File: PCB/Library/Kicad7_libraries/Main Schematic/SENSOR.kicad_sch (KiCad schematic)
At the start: 15 parts, among them Q1 2SC1815, Q2 2SC1815, U2 TMP100, U3 EA_T123X-I2C

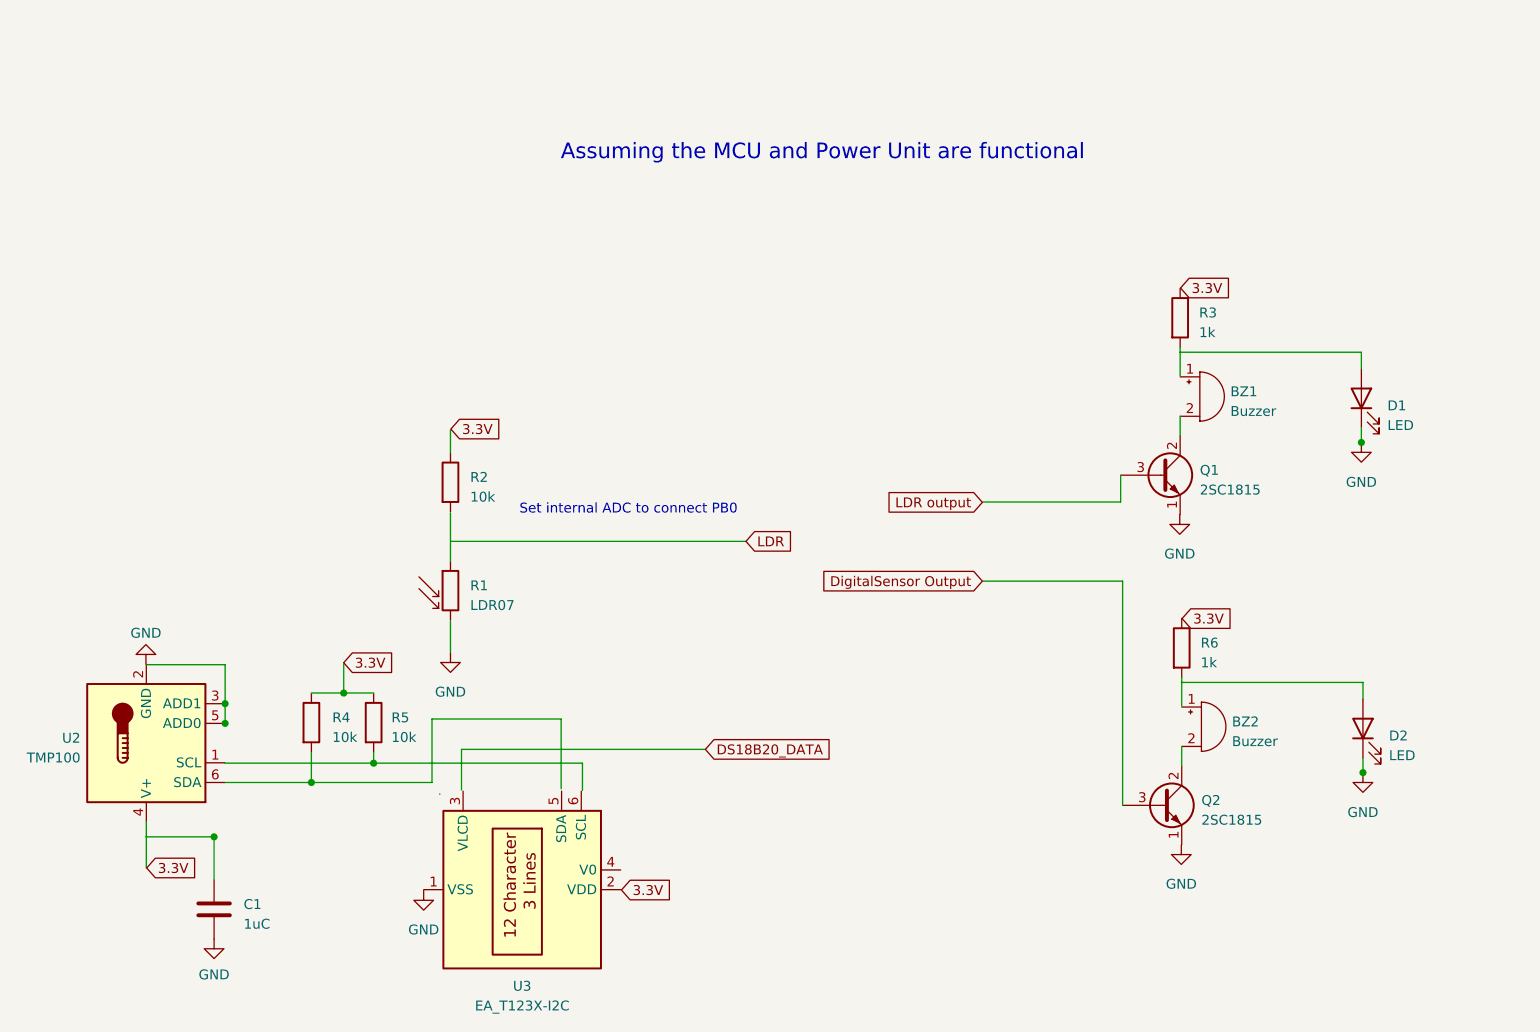
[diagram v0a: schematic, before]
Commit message: I recreated our schematics into hierachy sheets instead of individual sheets
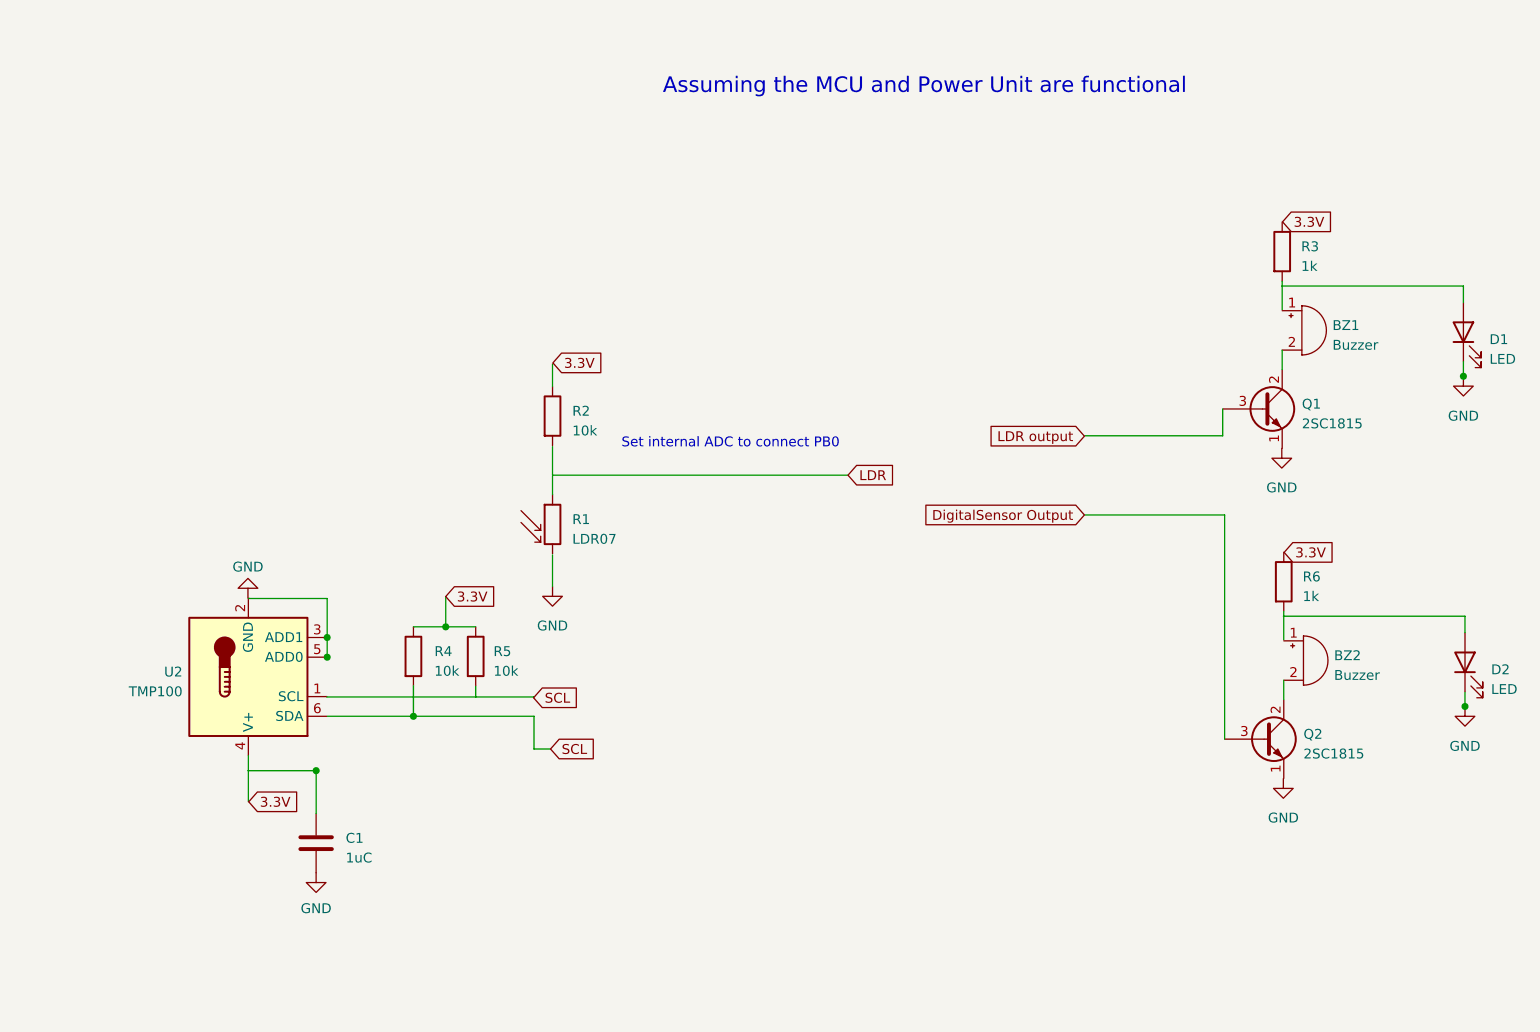
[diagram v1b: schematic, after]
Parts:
- removed U3: EA_T123X-I2C, Display:EA_T123X-I2C, symbol Display_Character:EA_T123X-I2C
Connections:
- net SCL: now reaches R4.2

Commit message: I have made the sensor wiring clearer
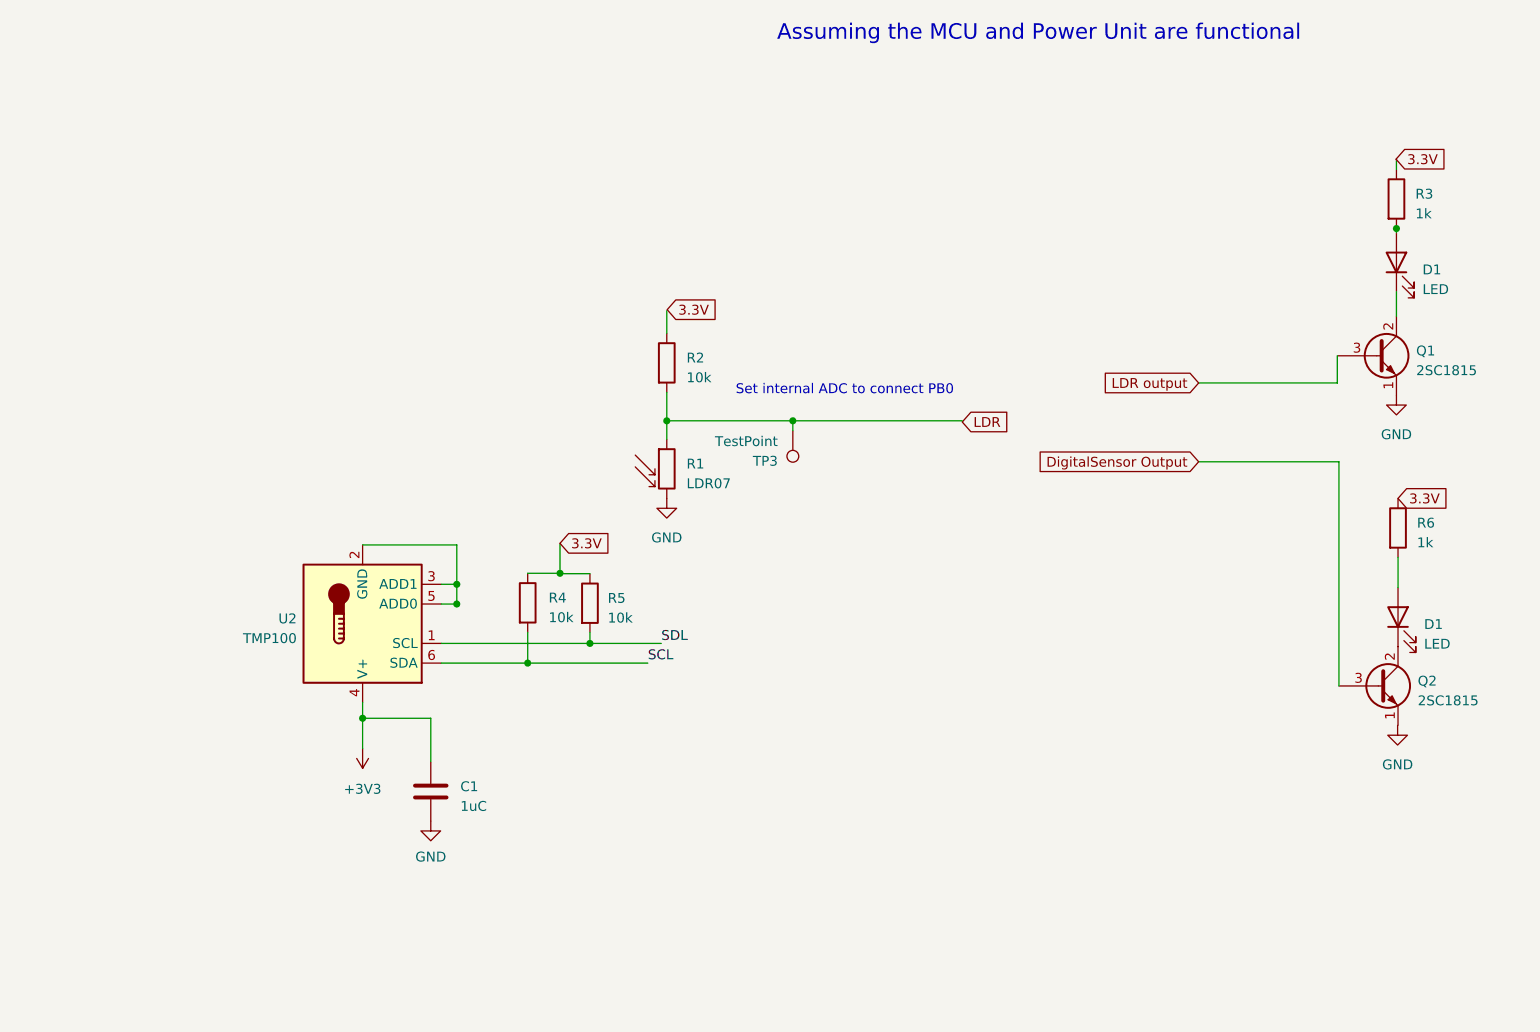
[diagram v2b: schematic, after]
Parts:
- removed BZ1, BZ2: Buzzer, symbol Device:Buzzer
- removed D1, D2: LED, symbol Device:LED
- added D1 (x2): LED, symbol Device:LED
- added TP3: TestPoint, symbol Connector:TestPoint
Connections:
- net 3.3V: now also R3.1, R6.1
- net GND: now also Q1.1 (E), R1.2
- net LDR output: now also Q1.3 (B)
- net SCL: now also U2.6 (SDA)
- net at Q1.2 (C): now also D1.1 (K)
- net at R3.2: now also D1.2 (A)
- net at R5.2: now also U2.1 (SCL)
- net +3V3: now reaches C1.1
- net +3V3: now also U2.4 (V+)
- net at R6.2: now also D1.2 (A)
- net at Q2.2 (C): now also D1.1 (K)
- net at R1.1: now also R2.2, TP3.1
- net at U2.2 (GND): now also U2.3 (ADD1), U2.5 (ADD0)
